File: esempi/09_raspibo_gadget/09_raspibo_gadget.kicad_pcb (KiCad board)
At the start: 2 copper layers, 25.4 x 25.4 mm, 24 parts, among them IC1 ATTINY85-S, P1 USB_OTG, P2 CONN_01X01, P3 CONN_01X01, P4 CONN_01X01, P5 CONN_01X01, P6 CONN_01X01, P7 CONN_01X01, P8 CONN_01X01, P9 CONN_01X01

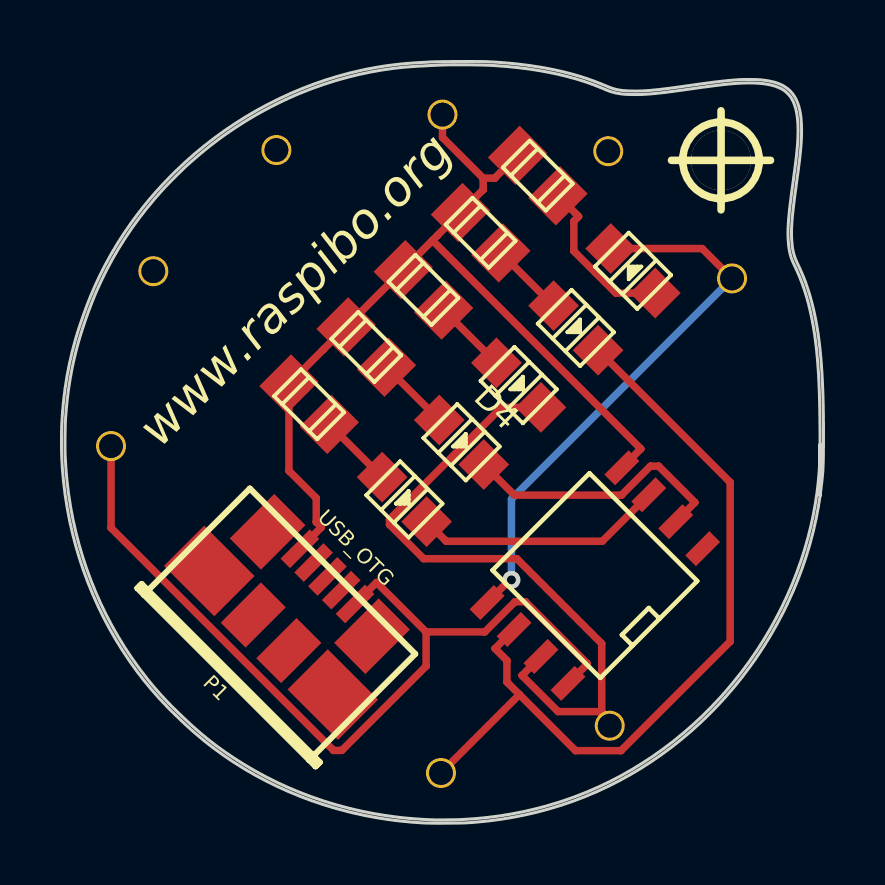
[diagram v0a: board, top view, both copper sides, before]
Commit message: Modifiche a Raspibo gadget e L293D
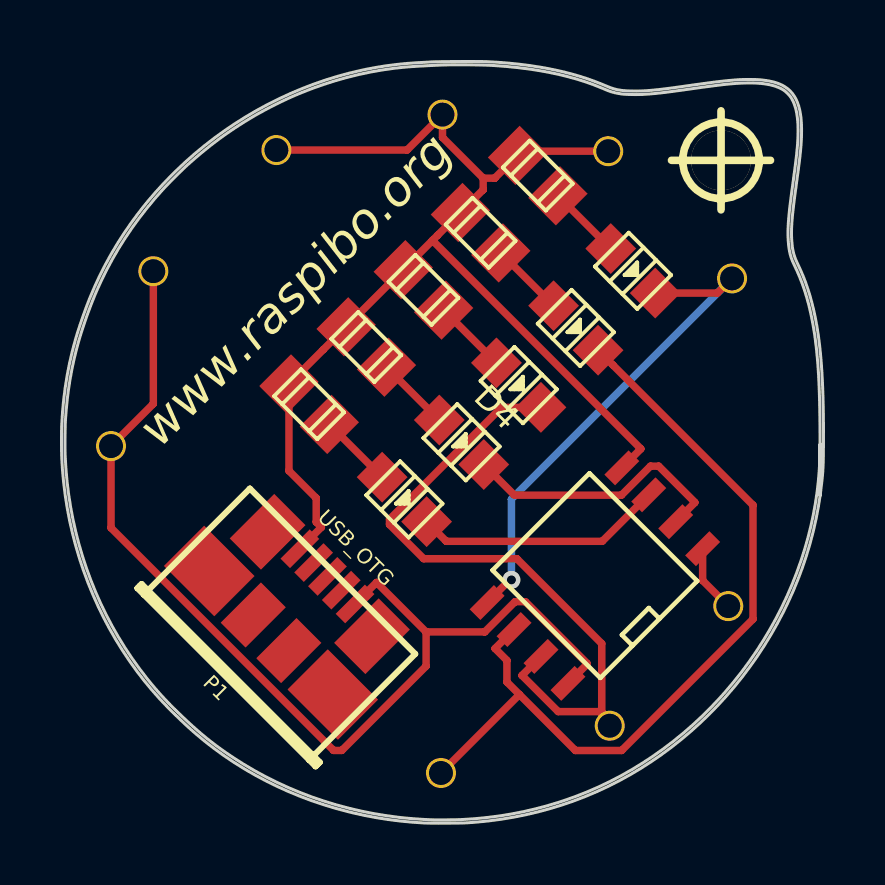
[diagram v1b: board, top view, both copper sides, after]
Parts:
- added P10: CONN_01X01, w_details:hole_1mm, F.Cu at (209.6, 84.8)
- turned D1 to 315 degrees
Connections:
- net Net-(D1-Pad2) renamed /MOSI
- net Net-(D2-Pad2) renamed /MISO
- net Net-(D3-Pad2) renamed /SCK
- IC1 pad 1: Net-(IC1-Pad1) -> /RESET
- P1 pad 1: GND -> VCC
- P1 pad 2: (no net) -> Net-(P1-Pad2)
- P1 pad 3: (no net) -> Net-(P1-Pad3)
- P1 pad 4: (no net) -> Net-(P1-Pad4)
- P1 pad 5: VCC -> GND
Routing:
- net GND: track 30.6 -> 64.6 mm
- net VCC: track 29.5 -> 11.1 mm
- net Net-(D1-Pad1): track 5.49 -> 2.68 mm
- net /RESET: track 0.00 -> 2.27 mm
- net /MOSI: track 18.7 -> 17.0 mm
- net /MISO: track 27.3 -> 27.9 mm
